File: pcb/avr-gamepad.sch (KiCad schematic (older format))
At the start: 34 parts, among them J1 Conn_01x08, J2 Conn_01x08, J3 Conn_01x08_Female, P1 USB_C_Plug_USB2.0, SW1 RESET, SW10 Up, SW11 Down, SW12 Left, SW13 Select, SW14 HWB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

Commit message: tweak gamepad shell triggers, button holes, and faceplate pegs. 45 degree cut PCB corners. test add ffc connector for joystick
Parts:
- J3: value Conn_01x08_Female -> Conn_01x05; footprint Connector_PinHeader_2.54mm:PinHeader_1x08_P2.54mm_Vertical -> Connector_FFC-FPC:Hirose_FH12-6S-0.5SH_1x06-1MP_P0.50mm_Horizontal; symbol Connector:Conn_01x08_Female -> Connector_Generic:Conn_01x05
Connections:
- wire segments 139 -> 141
- no-connect marks 4 -> 7
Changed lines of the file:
@@
 Text Label 5100 4300 0    50   ~ 0
 pe6-1
-$Comp
-L Connector:Conn_01x08_Female J3
-U 1 1 5DA62D9E
-P 5750 3550
-F 0 "J3" H 5642 4035 50  0000 C CNN
-F 1 "Conn_01x08_Female" H 5642 3944 50  0000 C CNN
-F 2 "Connector_PinHeader_2.54mm:PinHeader_1x08_P2.54mm_Vertical" H 5750 3550 50  0001 C CNN
-F 3 "~" H 5750 3550 50  0001 C CNN
-	1    5750 3550
-	-1   0    0    -1
-$EndComp
 Text Label 6800 4900 0    50   ~ 0
 pc7-32
@@
 Text Label 6800 4400 0    50   ~ 0
 pd7-27
-Text Label 5950 3550 0    50   ~ 0
-pd4-25
-Text Label 5950 3350 0    50   ~ 0
-pd3-21
-Text Label 5950 3250 0    50   ~ 0
-pd2-20
-Text Label 5950 3450 0    50   ~ 0
-pd5-22
 Text Label 5900 2700 0    50   ~ 0
 pd1-19
@@
 Text Label 5900 2400 0    50   ~ 0
 pb3-11
-Text Label 5950 3650 0    50   ~ 0
-pf7-36
-Text Label 5950 3850 0    50   ~ 0
-pf5-38
-Text Label 5950 3950 0    50   ~ 0
-pf4-39
 NoConn ~ 5100 4500
 NoConn ~ 5100 4600
@@
 pb0-8
 NoConn ~ 5100 4300
-Text Label 5950 3750 0    50   ~ 0
+NoConn ~ 8050 3400
+Text Label 6100 3050 0    50   ~ 0
 pf6-37
-NoConn ~ 8050 3400
+Text Label 6100 4550 0    50   ~ 0
+pf4-39
+Text Label 6100 4450 0    50   ~ 0
+pf5-38
+Text Label 6100 3350 0    50   ~ 0
+pf7-36
+Text Label 6100 4050 0    50   ~ 0
+pd5-22
+Text Label 6100 3250 0    50   ~ 0
+pd2-20
+Text Label 6100 3950 0    50   ~ 0
+pd3-21
+Text Label 6100 4150 0    50   ~ 0
+pd4-25
+$Comp
+L power:GND #PWR?
+U 1 1 5E1C2864
+P 6550 3150
+F 0 "#PWR?" H 6550 2900 50  0001 C CNN
+F 1 "GND" H 6555 2977 50  0000 C CNN
+F 2 "" H 6550 3150 50  0001 C CNN
+F 3 "" H 6550 3150 50  0001 C CNN
+	1    6550 3150
+	1    0    0    -1
+$EndComp
+$Comp
+L power:VCC #PWR?
+U 1 1 5E1D50BD
+P 6400 3450
+F 0 "#PWR?" H 6400 3300 50  0001 C CNN
+F 1 "VCC" H 6417 3623 50  0000 C CNN
+F 2 "" H 6400 3450 50  0001 C CNN
+F 3 "" H 6400 3450 50  0001 C CNN
+	1    6400 3450
+	1    0    0    -1
+$EndComp
+$Comp
+L Connector_Generic:Conn_01x05 J3
+U 1 1 5DA62D9E
+P 5900 3250
+F 0 "J3" H 5792 3735 50  0000 C CNN
+F 1 "Conn_01x05" H 5792 3644 50  0000 C CNN
+F 2 "Connector_FFC-FPC:Hirose_FH12-6S-0.5SH_1x06-1MP_P0.50mm_Horizontal" H 5900 3250 50  0001 C CNN
+F 3 "~" H 5900 3250 50  0001 C CNN
+	1    5900 3250
+	-1   0    0    1
+$EndComp
+Wire Wire Line
+	6100 3150 6550 3150
+Wire Wire Line
+	6100 3450 6400 3450
+NoConn ~ 6100 3950
+NoConn ~ 6100 4050
+NoConn ~ 6100 4150
 $EndSCHEMATC

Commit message: cleanup schematic
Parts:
- U1: symbol MCU_Microchip_ATmega:ATmega32U4-AU -> avr-gamepad-rescue:ATmega32U4-AU-MCU_Microchip_ATmega
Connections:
- net labels added: D+, D-
- wire segments 141 -> 146
- no-connect marks 7 -> 4
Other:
- moved on the sheet: C1, C2, C3, C4, C5, C6, D1, D2, J1, J2, J3, P1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

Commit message: full matrix
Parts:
- added D10, D11, D12, D13, D14, D15, D16, D17, D18, D3, D4, D5, D6, D7, D8, D9: 1N4148, Diode_THT:D_DO-35_SOD27_P7.62mm_Horizontal, symbol Diode:1N4148
- added J4: Conn_01x05, Connector_FFC-FPC:Hirose_FH12-6S-0.5SH_1x06-1MP_P0.50mm_Horizontal, symbol Connector_Generic:Conn_01x05
- added SW13: Left, button-contacts:Small, symbol Switch:SW_Push
- added SW14: Right, button-contacts:Large_tapered, symbol Switch:SW_Push
- added SW15: Y, button-contacts:Large_tapered, symbol Switch:SW_Push
- added SW16: A, button-contacts:Large_tapered, symbol Switch:SW_Push
- J1, J2: value Conn_01x08 -> Conn_01x12; symbol Connector_Generic:Conn_01x08 -> Connector_Generic:Conn_01x12
- SW10: value Up -> R1
- SW11: value Down -> R2
- SW12: value Left -> X
- SW17: renamed from SW13; value Select -> Start
- SW2: value R -> Select
- SW3: value X -> Custom
- SW4: value A -> L1
- SW5: value B -> L2
- SW6: value Start -> Up
- SW7: value Y -> Down
- SW8: value Right -> Custom2
- SW9: value L -> B
- renumbered SW14 to SW18
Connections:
- net pd5-22 is gone; now on net LEDLeft: U1.22 (PD5)
- net +5V: now also J2.11 (Pin_11)
- net GND: now also J2.12 (Pin_12), Y1.4; no longer J2.8 (Pin_8), SW2.2, SW3.2, SW4.2, SW5.2, SW6.2, SW7.2
- net ColR3: now reaches SW17.1
- net ColR3: now also J1.6 (Pin_6), SW10.1, SW11.1, SW8.1; no longer J1.1 (Pin_1)
- net RowR2: now reaches J1.2 (Pin_2)
- net RowR2: now also D12.1 (K), D16.1 (K); no longer SW8.1
- net RowR3: now reaches J1.3 (Pin_3)
- net RowR3: now also D13.1 (K), D17.1 (K); no longer SW10.1
- net RowR4: now reaches J1.4 (Pin_4)
- net RowR4: now also D14.1 (K), D18.1 (K); no longer SW11.1
- net ColR4: now reaches J1.5 (Pin_5), SW12.1
- net ColR4: now also SW9.1, SW15.1, SW16.1
- net at R6.2: now also J1.10 (Pin_10); no longer J1.7 (Pin_7)
- net pb0-8: no longer names the net of U1.8 (PB0)
- net pb0-8: no longer SW2.1
- net pb1-9: no longer names the net of U1.9 (PB1)
- net pb1-9: no longer SW3.1
- net pb2-10: no longer names the net of U1.10 (PB2)
- net pb2-10: no longer SW4.1
- net pb3-11: no longer names the net of U1.11 (PB3)
- net pb3-11: no longer SW5.1
- net pb4-28 renamed Col3
- net Col3: now also J2.6 (Pin_6); no longer J2.3 (Pin_3)
- net pb5-29 renamed Col4
- net Col4: now also J2.5 (Pin_5); no longer J2.4 (Pin_4)
- net pb6-30 renamed L3
- net L3: now also J3.3 (Pin_3); no longer J2.5 (Pin_5)
- net pb7-12 renamed Col1
- net Col1: now also SW7.1, U1.27 (PD7), SW13.1, SW14.1; no longer U1.12 (PB7)
- net pc6-31 renamed Row4
- net Row4: now also J2.4 (Pin_4), D10.1 (K), D6.1 (K); no longer J2.6 (Pin_6)
- net pc7-32 renamed JoyRightX
- net JoyRightX: now also U1.37 (PF6); no longer U1.32 (PC7)
- net pd0-18 renamed Row2
- net Row2: now also J2.2 (Pin_2), D4.1 (K), D8.1 (K); no longer SW7.1
- net pd1-19 renamed LEDLeft
- net LEDLeft: no longer U1.19 (PD1)
- net pd2-20: no longer names the net of U1.20 (PD2)
- net pd2-20: no longer J3.3 (Pin_3)
- net pd3-21: no longer names the net of U1.21 (PD3)
- net pd4-25 renamed Row3
- net Row3: now also J2.3 (Pin_3), D5.1 (K), D9.1 (K)
- net pd6-26: no longer names the net of U1.26 (PD6)
- net pd6-26: no longer J2.1 (Pin_1)
- removed net pd7-27: J2.2 (Pin_2), U1.27 (PD7)
- net pe6-1 renamed Col2
- net Col2: now also SW2.1, SW3.1, SW4.1, SW5.1
- net pf0-41: no longer names the net of U1.41 (PF0)
- net pf1-40: no longer names the net of U1.40 (PF1)
- net pf4-39 renamed JoyLeftX
- net JoyLeftX: now also J3.5 (Pin_5)
- net pf5-38 renamed JoyLeftY
- net JoyLeftY: now also J3.2 (Pin_2)
- removed net pf6-37: J3.5 (Pin_5), U1.37 (PF6)
- net pf7-36 renamed JoyRightY
- net JoyRightY: now also J2.8 (Pin_8); no longer J3.2 (Pin_2)
- new net: D7.2 (A), SW2.2
- new net: D8.2 (A), SW3.2
- new net: D9.2 (A), SW4.2
- new net: D10.2 (A), SW5.2
- new net: D3.2 (A), SW6.2
- new net: D4.2 (A), SW7.2
- new net: J1.7 (Pin_7), J4.5 (Pin_5)
- new net: J1.8 (Pin_8), J4.2 (Pin_2)
- new net: J1.9 (Pin_9), J4.3 (Pin_3)
- new net: D11.2 (A), SW17.2
- new net: D15.2 (A), SW12.2
- new net: D14.2 (A), SW11.2
- new net: D13.2 (A), SW10.2
- new net: D16.2 (A), SW9.2
- new net: D12.2 (A), SW8.2
- new net: D17.2 (A), SW15.2
- new net: D18.2 (A), SW16.2
- new net: D6.2 (A), SW14.2
- new net: D5.2 (A), SW13.2
- new net GND_R: D2.2 (A), J1.12 (Pin_12), J4.4 (Pin_4)
- new net LEDRight: J2.10 (Pin_10), U1.32 (PC7)
- new net R3: J2.9 (Pin_9), U1.12 (PB7)
- new net Row1: D3.1 (K), D7.1 (K), J2.1 (Pin_1), U1.19 (PD1)
- new net RowR1: D11.1 (K), D15.1 (K), J1.1 (Pin_1)
- new net VCC_R: J1.11 (Pin_11), J4.1 (Pin_1)
- no-connect marks 4 -> 9
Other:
- moved on the sheet: D1, D2, J3, R5, R6, SW10, SW11, SW12, SW17, SW18, SW2, SW3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

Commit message: switched to pcf8574
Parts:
- removed SW12: X, button-contacts:Large_tapered, symbol Switch:SW_Push
- added D19, D20: 1N4148, Diode_THT:D_DO-35_SOD27_P7.62mm_Horizontal, symbol Diode:1N4148
- added R10, R7, R8, R9: 1K, Resistor_SMD:R_0805_2012Metric, symbol Device:R
- added SW19: X, button-contacts:Small, symbol Switch:SW_Push
- added SW20: Custom2, button-contacts:Large_tapered, symbol Switch:SW_Push
- added U2, U3: PCF8574, symbol Interface_Expansion:PCF8574
- J1, J2: value Conn_01x12 -> Conn_01x06; symbol Connector_Generic:Conn_01x12 -> Connector_Generic:Conn_01x06
- SW10: value R1 -> R2
- SW11: value R2 -> A
- SW14: value Right -> L2
- SW15: value Y -> Custom4
- SW16: value A -> B
- SW17: footprint button-contacts:Small -> button-contacts:Large_tapered
- SW18: value HWB -> Y; footprint button-contacts:Small -> button-contacts:Large_tapered
- SW2: value Select -> Right
- SW3: value Custom -> Up
- SW4: value L1 -> Down
- SW5: value L2 -> Custom1
- SW6: value Up -> Select
- SW7: value Down -> L1
- SW8: value Custom2 -> R1; footprint button-contacts:Large_tapered -> button-contacts:Small
- SW9: value B -> Custom3
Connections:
- net +5V: now also J2.5 (Pin_5), R7.1, R8.1, U3.16 (VDD); no longer J2.11 (Pin_11)
- net Col1: now also U3.7 (P3); no longer SW6.1, U1.27 (PD7)
- net Col2: now also U3.9 (P4); no longer SW2.1, U1.1 (PE6)
- net Col3: now also SW2.1, SW6.1, SW20.1, U3.10 (P5); no longer J2.6 (Pin_6), U1.28 (PB4)
- net ColR3: now also SW15.1, SW18.1, SW19.1, U2.10 (P5); no longer J1.6 (Pin_6), SW10.1, SW11.1, SW17.1, SW8.1
- net GND: now also J2.6 (Pin_6), U3.1 (A0), U3.2 (A1), U3.3 (A2), U3.8 (VSS); no longer J2.12 (Pin_12), SW18.2
- net GND_R: now also J1.6 (Pin_6), U2.8 (VSS); no longer J1.12 (Pin_12)
- net JoyRightX: now also J2.3 (Pin_3); no longer J2.7 (Pin_7)
- net JoyRightY: now also J2.4 (Pin_4); no longer J2.8 (Pin_8)
- net L3: now also U3.11 (P6); no longer U1.30 (PB6)
- net R3: now also J4.3 (Pin_3), U2.11 (P6); no longer J2.9 (Pin_9), U1.12 (PB7)
- net Row1: now also D4.1 (K), D8.1 (K), U3.4 (P0); no longer D7.1 (K), J2.1 (Pin_1), U1.19 (PD1)
- net Row2: now also D5.1 (K), D7.1 (K), D9.1 (K), U3.5 (P1); no longer D4.1 (K), D8.1 (K), J2.2 (Pin_2), U1.18 (PD0)
- net Row3: now also D10.1 (K), D6.1 (K), D20.1 (K), U3.6 (P2); no longer D5.1 (K), D9.1 (K), J2.3 (Pin_3), U1.25 (PD4)
- net RowR1: now also D14.1 (K), D17.1 (K), U2.4 (P0); no longer D15.1 (K), J1.1 (Pin_1)
- net RowR2: now also D15.1 (K), D18.1 (K), U2.5 (P1); no longer D16.1 (K), J1.2 (Pin_2)
- net RowR3: now also D16.1 (K), D19.1 (K), U2.6 (P2); no longer D17.1 (K), J1.3 (Pin_3)
- net VCC_R: now also J1.5 (Pin_5), R10.1, R9.1, U2.16 (VDD); no longer J1.11 (Pin_11)
- net at U1.33 (~HWB~/PE2): no longer SW18.1
- net at R6.2: now also U2.12 (P7); no longer J1.10 (Pin_10)
- net JoyRightX_R: now reaches J4.5 (Pin_5)
- net JoyRightX_R: now also J1.3 (Pin_3); no longer J1.7 (Pin_7)
- net JoyRightY_R: now reaches J4.2 (Pin_2)
- net JoyRightY_R: now also J1.4 (Pin_4); no longer J1.8 (Pin_8)
- net at D15.2 (A): now also SW16.2
- net at SW15.2: now also D19.2 (A); no longer D17.2 (A)
- net at D18.2 (A): now also SW18.2; no longer SW16.2
- net Col4: no longer names the net of U1.29 (PB5)
- net Col4: no longer J2.5 (Pin_5)
- net ColR4 renamed ColR2
- net ColR2: now also SW11.1, U2.9 (P4); no longer J1.5 (Pin_5), SW15.1
- net LEDLeft: no longer names the net of U1.22 (PD5)
- net LEDLeft: no longer R5.2
- net LEDRight: no longer names the net of U1.32 (PC7)
- net LEDRight: no longer J2.10 (Pin_10)
- removed net Row4: D10.1 (K), D6.1 (K), J2.4 (Pin_4), U1.31 (PC6)
- removed net RowR4: D14.1 (K), D18.1 (K), J1.4 (Pin_4)
- new net: R5.2, U3.12 (P7)
- new net: D20.2 (A), SW20.2
- new net: D17.2 (A), SW19.2
- new net ColR1: SW10.1, SW17.1, SW8.1, U2.7 (P3)
- new net SCL: J2.2 (Pin_2), R7.2, U1.18 (PD0), U3.14 (SCL)
- new net SCL_R: J1.2 (Pin_2), R10.2, U2.14 (SCL)
- new net SDA: J2.1 (Pin_1), R8.2, U1.19 (PD1), U3.15 (SDA)
- new net SDA_R: J1.1 (Pin_1), R9.2, U2.15 (SDA)
- no-connect marks 9 -> 25
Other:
- moved on the sheet: D10, D2, D3, D4, D5, D6, D7, D8, D9, J3, J4, R6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

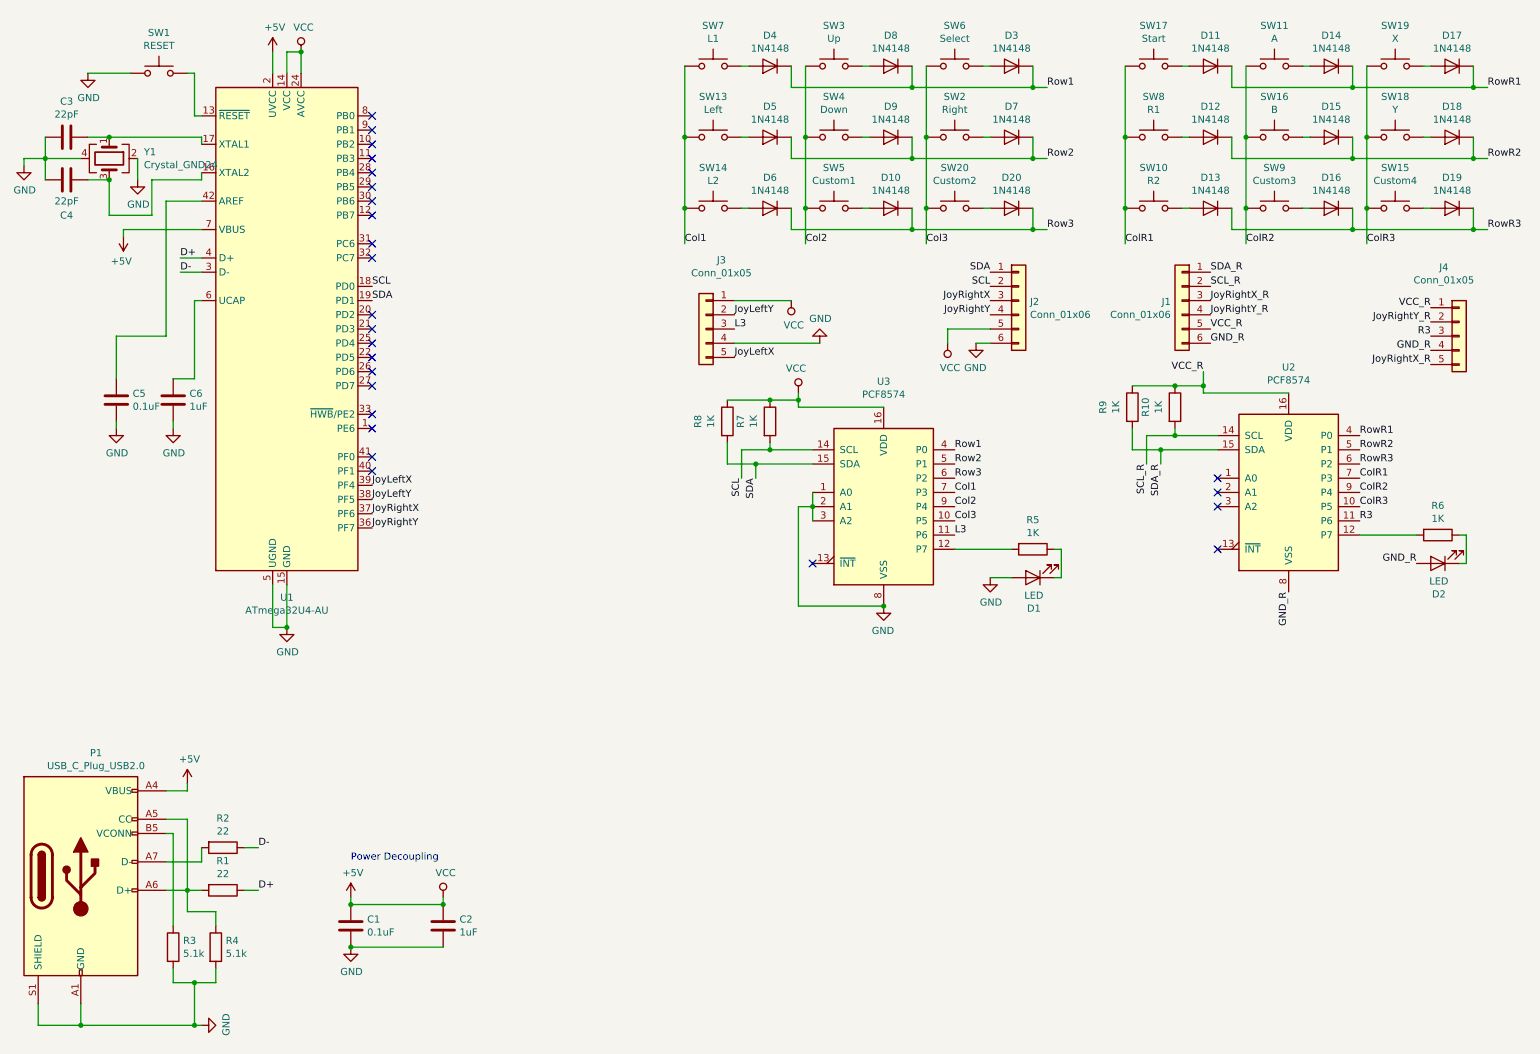
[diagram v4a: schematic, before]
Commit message: change left/right on schematic, start arranging pcb, add pcf8574 footprint
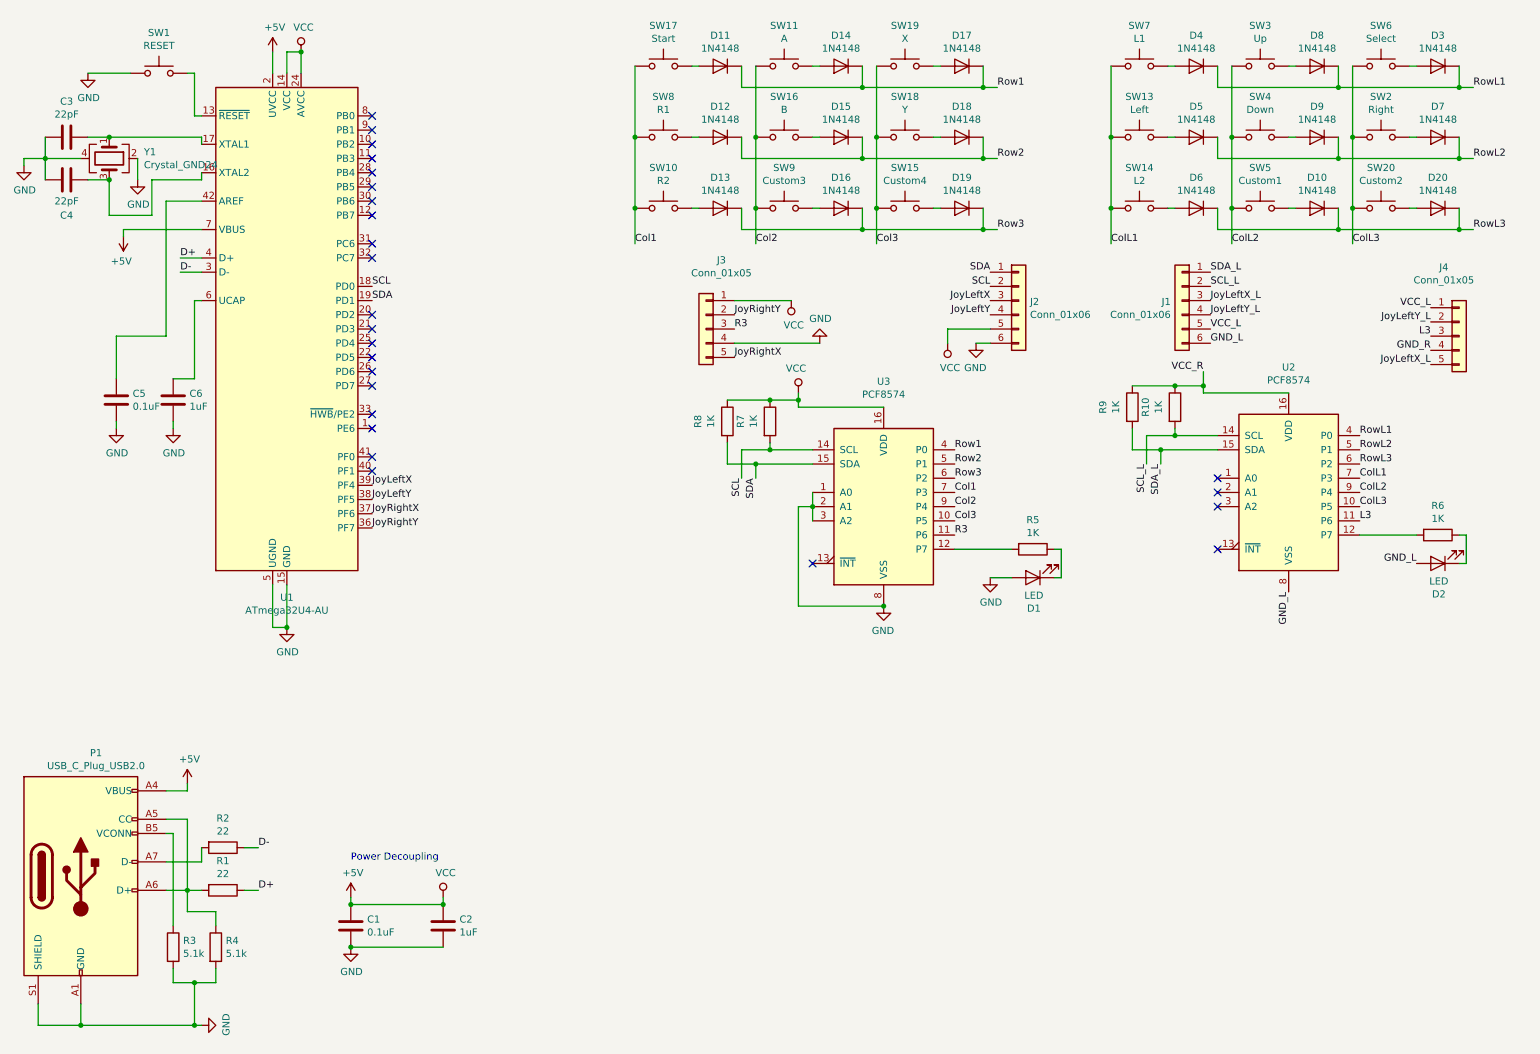
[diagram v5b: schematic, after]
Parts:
- C1, C2, C3, C4, C5, C6: footprint Capacitor_SMD:C_0805_2012Metric -> Capacitor_SMD:C_0603_1608Metric
- D1, D2: footprint LED_SMD:LED_0805_2012Metric -> LED_SMD:LED_0603_1608Metric
- D10, D11, D12, D13, D14, D15, D16, D17, D18, D19, D20, D3, D4, D5, D6, D7, D8, D9: footprint Diode_THT:D_DO-35_SOD27_P7.62mm_Horizontal -> Diode_SMD:D_0603_1608Metric
- J3, J4: footprint Connector_FFC-FPC:Hirose_FH12-6S-0.5SH_1x06-1MP_P0.50mm_Horizontal -> uxcell-ffc:uxcell_ffc_0.5pitch_1x05
- R1, R10, R2, R3, R4, R5, R6, R7, R8, R9: footprint Resistor_SMD:R_0805_2012Metric -> Resistor_SMD:R_0603_1608Metric
- SW10, SW14, SW15, SW17, SW20, SW9: footprint button-contacts:Large_tapered -> button-contacts:Small
- SW13, SW19: footprint button-contacts:Small -> button-contacts:Large_tapered
- U2, U3: footprint (none) -> pcf8574:SO16W
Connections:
- net Col1: now also SW10.1, SW17.1, SW8.1; no longer SW13.1, SW14.1, SW7.1
- net Col2: now also SW11.1, SW16.1, SW9.1; no longer SW3.1, SW4.1, SW5.1
- net Col3: now also SW15.1, SW18.1, SW19.1; no longer SW2.1, SW20.1, SW6.1
- net GND_R: no longer D2.2 (A), J1.6 (Pin_6), U2.8 (VSS)
- net JoyLeftX: now also J2.3 (Pin_3); no longer J3.5 (Pin_5)
- net JoyLeftY: now also J2.4 (Pin_4); no longer J3.2 (Pin_2)
- net JoyRightX: now also J3.5 (Pin_5); no longer J2.3 (Pin_3)
- net JoyRightY: now also J3.2 (Pin_2); no longer J2.4 (Pin_4)
- net L3: now also J4.3 (Pin_3), U2.11 (P6); no longer J3.3 (Pin_3), U3.11 (P6)
- net R3: now also J3.3 (Pin_3), U3.11 (P6); no longer J4.3 (Pin_3), U2.11 (P6)
- net Row1: now also D11.1 (K), D14.1 (K), D17.1 (K); no longer D3.1 (K), D4.1 (K), D8.1 (K)
- net Row2: now also D12.1 (K), D15.1 (K), D18.1 (K); no longer D5.1 (K), D7.1 (K), D9.1 (K)
- net Row3: now also D13.1 (K), D16.1 (K), D19.1 (K); no longer D10.1 (K), D20.1 (K), D6.1 (K)
- net VCC_R: no longer J1.5 (Pin_5), J4.1 (Pin_1)
- removed net ColR1: SW10.1, SW17.1, SW8.1, U2.7 (P3)
- removed net ColR2: SW11.1, SW16.1, SW9.1, U2.9 (P4)
- removed net ColR3: SW15.1, SW18.1, SW19.1, U2.10 (P5)
- net JoyRightX_R renamed JoyLeftX_L
- net JoyRightY_R renamed JoyLeftY_L
- removed net RowR1: D11.1 (K), D14.1 (K), D17.1 (K), U2.4 (P0)
- removed net RowR2: D12.1 (K), D15.1 (K), D18.1 (K), U2.5 (P1)
- removed net RowR3: D13.1 (K), D16.1 (K), D19.1 (K), U2.6 (P2)
- net SCL_R renamed SCL_L
- net SDA_R renamed SDA_L
- new net ColL1: SW13.1, SW14.1, SW7.1, U2.7 (P3)
- new net ColL2: SW3.1, SW4.1, SW5.1, U2.9 (P4)
- new net ColL3: SW2.1, SW20.1, SW6.1, U2.10 (P5)
- new net GND_L: D2.2 (A), J1.6 (Pin_6), U2.8 (VSS)
- new net RowL1: D3.1 (K), D4.1 (K), D8.1 (K), U2.4 (P0)
- new net RowL2: D5.1 (K), D7.1 (K), D9.1 (K), U2.5 (P1)
- new net RowL3: D10.1 (K), D20.1 (K), D6.1 (K), U2.6 (P2)
- new net VCC_L: J1.5 (Pin_5), J4.1 (Pin_1)
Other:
- moved on the sheet: D10, D11, D12, D13, D14, D15, D16, D17, D18, D19, D20, D3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
